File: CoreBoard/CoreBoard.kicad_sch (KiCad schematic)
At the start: 75 parts, among them J1 RJ45_LED_Shielded, SW1 SW_Push, SW10 SW_Push, SW12 SW_DIP_x07, SW2 SW_Push, SW3 SW_Push, SW4 SW_Push, SW5 SW_Push, SW6 SW_Push, SW7 SW_Push, SW8 SW_Push, SW9 SW_Push, U1 OKI, U2 Teensy4.1_DEV-16771, U3 SHHD003A0A, U4 GY-521, U5 ATA6561, U6 74HC148, U7 74HC148, U8 74HC00

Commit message: Fixed many things from schematic review, VCC power flags, no connects, added a 4th NAND gate, changed labels to text, changed DS8 tag to DS_EN, and removed the standby tag from the CAN transceiver to connect it to ground
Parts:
- added unit 4 of U8
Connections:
- net STBY is gone; now on net GND: U5.8 (STBY)
- net 5V: now also Conn2.1, U3.6 (Vout+)
- net DS8 renamed DS_EN
- net DS_EN: now also U6.12 (I2); no longer U2.10 (CS1)
- net DS9: no longer names the net of U2.36 (CS2)
- net DS9: no longer U6.12 (I2)
- net PV renamed VCC
- no-connect marks 18 -> 31
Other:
- note added: "Accelerometer"
- note added: "Encoders"
- note added: "Gimbal Buttons"
- note added: "NeoPixels"
- note added: "Power"
- note added: "Power LED"
- note added: "Servo Communication"
- note added: "Teensy"
- note added: "VESC Serial"
- moved on the sheet: U8E

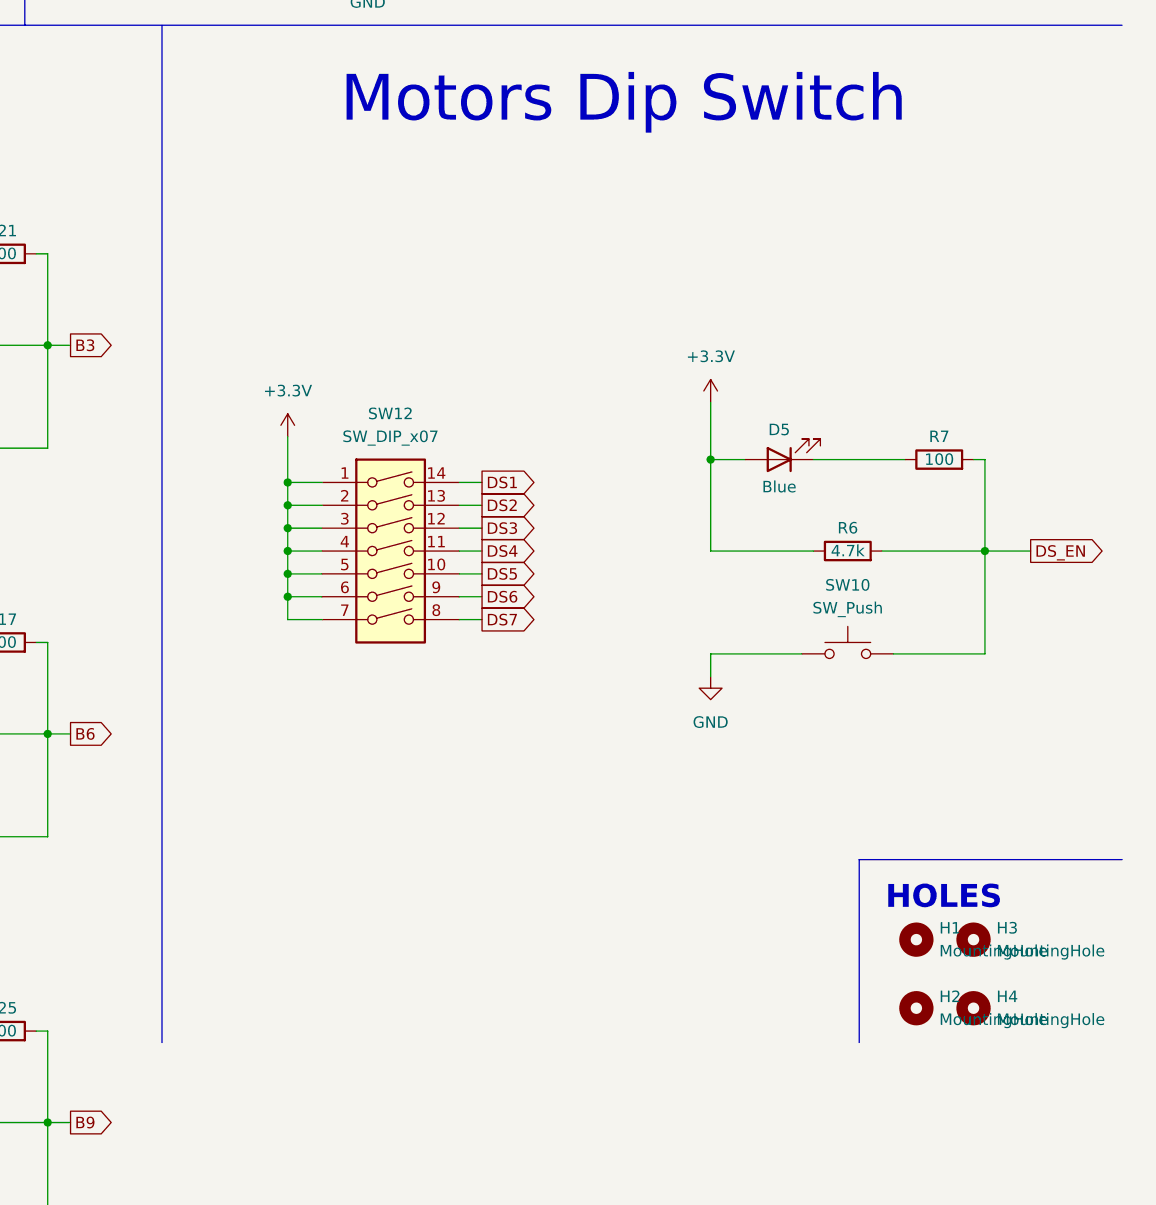
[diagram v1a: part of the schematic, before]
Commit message: Added CAN Connectors
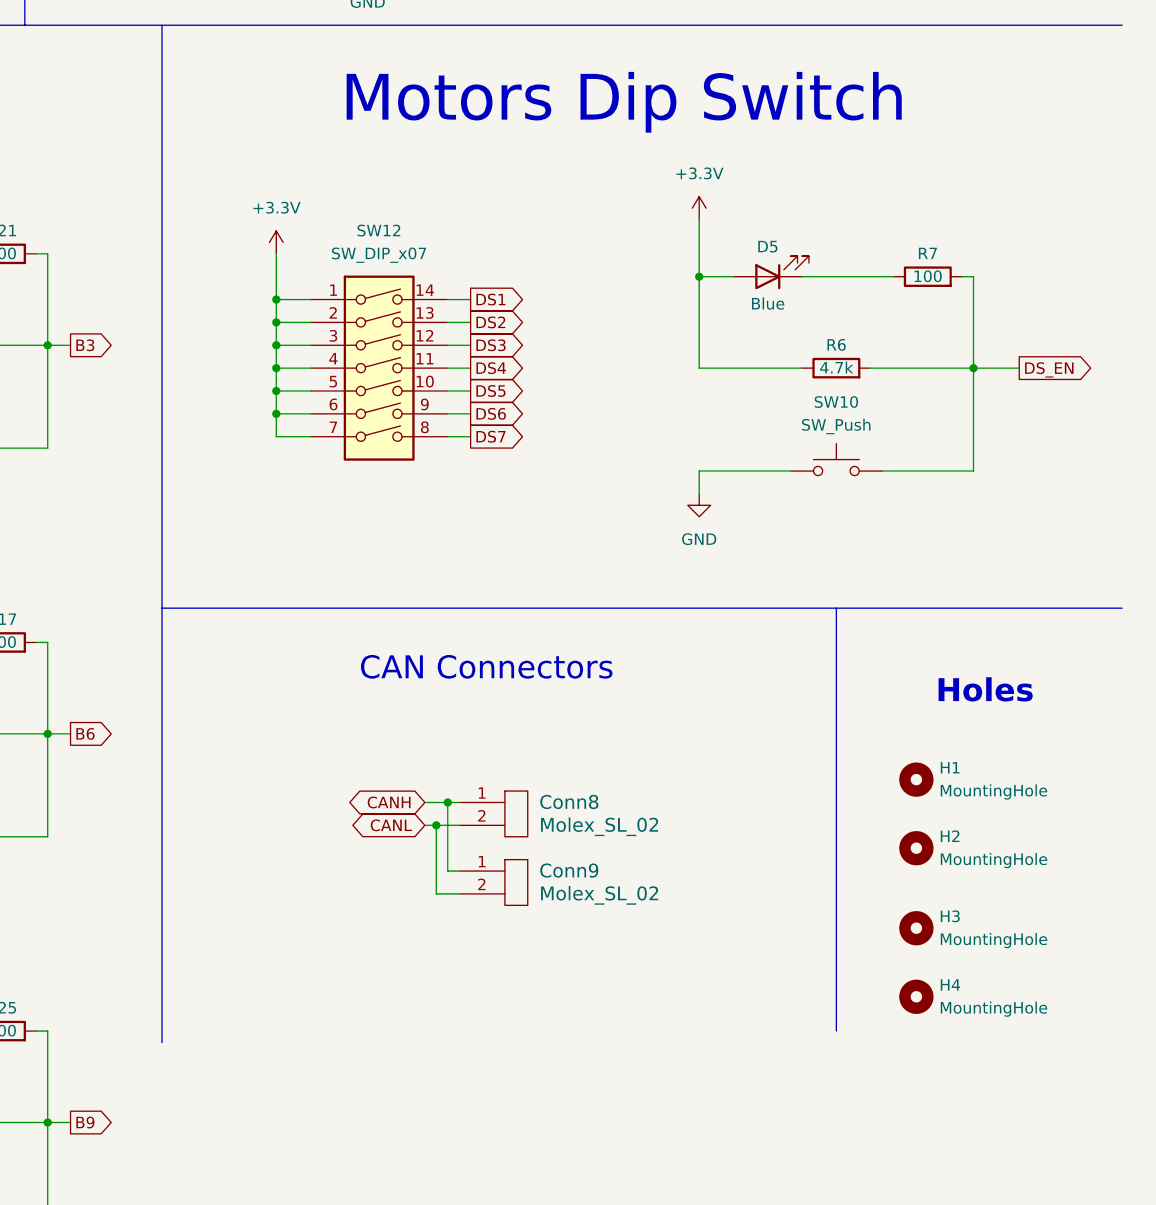
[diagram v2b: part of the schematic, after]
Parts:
- added Conn8, Conn9: Molex_SL_02, MRDT_Connectors:MOLEX_SL_02_Vertical, symbol MRDT_Connectors:Molex_SL_02
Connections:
- net CANH: now also Conn8.1, Conn9.1
- net CANL: now also Conn8.2, Conn9.2
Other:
- note added: "CAN Connectors"
- note added: "Holes"
- note removed: "HOLES"
- moved on the sheet: D5, H1, H2, H3, H4, R6, R7, SW10, SW12

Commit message: Added footprints to the majority of components on the schematic
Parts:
- C1: footprint (none) -> Capacitor_SMD:C_1206_3216Metric_Pad1.33x1.80mm_HandSolder
- C2, C3, C4, C5, C6: footprint (none) -> Capacitor_SMD:C_0603_1608Metric_Pad1.08x0.95mm_HandSolder
- Conn1: footprint (none) -> MRDT_Connectors:Square_Anderson_2_H_Side_By_Side_PV
- Conn2: footprint (none) -> MRDT_Connectors:MOLEX_SL_03_Vertical
- Conn3, Conn4, Conn5, Conn6, Conn7: footprint (none) -> MRDT_Connectors:MOLEX_SL_09_Horizontal
- D1, D10, D11, D12, D13, D2, D3, D4, D5, D6, D7, D8, D9: footprint (none) -> LED_SMD:LED_0603_1608Metric_Pad1.05x0.95mm_HandSolder
- J1: footprint (none) -> MRDT_Connectors:RJ45_Teensy
- R1, R10, R11, R12, R13, R14, R15, R16, R17, R18, R19, R2, R20, R21, R22, R23, R24, R25, R3, R4, R5, R6, R7, R8, R9: footprint (none) -> Resistor_SMD:R_0603_1608Metric_Pad0.98x0.95mm_HandSolder
- SW1, SW10, SW2, SW3, SW4, SW5, SW6, SW7, SW8, SW9: footprint (none) -> Button_Switch_SMD:SW_SPST_TL3305A
- U1: footprint (none) -> MRDT_Devices:OKI_Horizontal
- U2: footprint MODULE_DEV-16771 -> MRDT_Shields:Teensy_4_1_Ethernet
- U8: footprint (none) -> Package_SO:SO-14_5.3x10.2mm_P1.27mm

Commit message: Layout has been changed to group components together similar to the style of the schematic for better connections, and the footprint for the OKI for the NeoPixels has been changed
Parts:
- U3: footprint MRDT_Devices:SHHD003A0A-SRZ -> MRDT_Devices:SHHD003A0A-SRZ_Surface_Mount
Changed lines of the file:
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@@
 			)
 		)
-		(property "Footprint" "MRDT_Devices:SHHD003A0A-SRZ"
+		(property "Footprint" "MRDT_Devices:SHHD003A0A-SRZ_Surface_Mount"
 			(at 133.35 46.99 0)
 			(effects

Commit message: Added footprints for mounting holes
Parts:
- H1, H2, H3, H4: footprint (none) -> MRDT_Drill_Holes:4_40_Hole
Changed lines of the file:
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@@
 			)
 		)
-		(property "Footprint" ""
+		(property "Footprint" "MRDT_Drill_Holes:4_40_Hole"
 			(at 384.81 223.52 0)
 			(effects
@@
 			)
 		)
-		(property "Footprint" ""
+		(property "Footprint" "MRDT_Drill_Holes:4_40_Hole"
 			(at 384.81 240.03 0)
 			(effects
@@
 			)
 		)
-		(property "Footprint" ""
+		(property "Footprint" "MRDT_Drill_Holes:4_40_Hole"
 			(at 384.81 247.65 0)
 			(effects
@@
 			)
 		)
-		(property "Footprint" ""
+		(property "Footprint" "MRDT_Drill_Holes:4_40_Hole"
 			(at 384.81 231.14 0)
 			(effects

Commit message: Changed footprint of NeoPixels to a though hole, and added some wires
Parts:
- U3: footprint MRDT_Devices:SHHD003A0A-SRZ_Surface_Mount -> MRDT_Devices:SHHD003A0A41Z_Through_Hole
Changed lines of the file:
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@@
 			)
 		)
-		(property "Footprint" "MRDT_Devices:SHHD003A0A-SRZ_Surface_Mount"
+		(property "Footprint" "MRDT_Devices:SHHD003A0A41Z_Through_Hole"
 			(at 133.35 46.99 0)
 			(effects

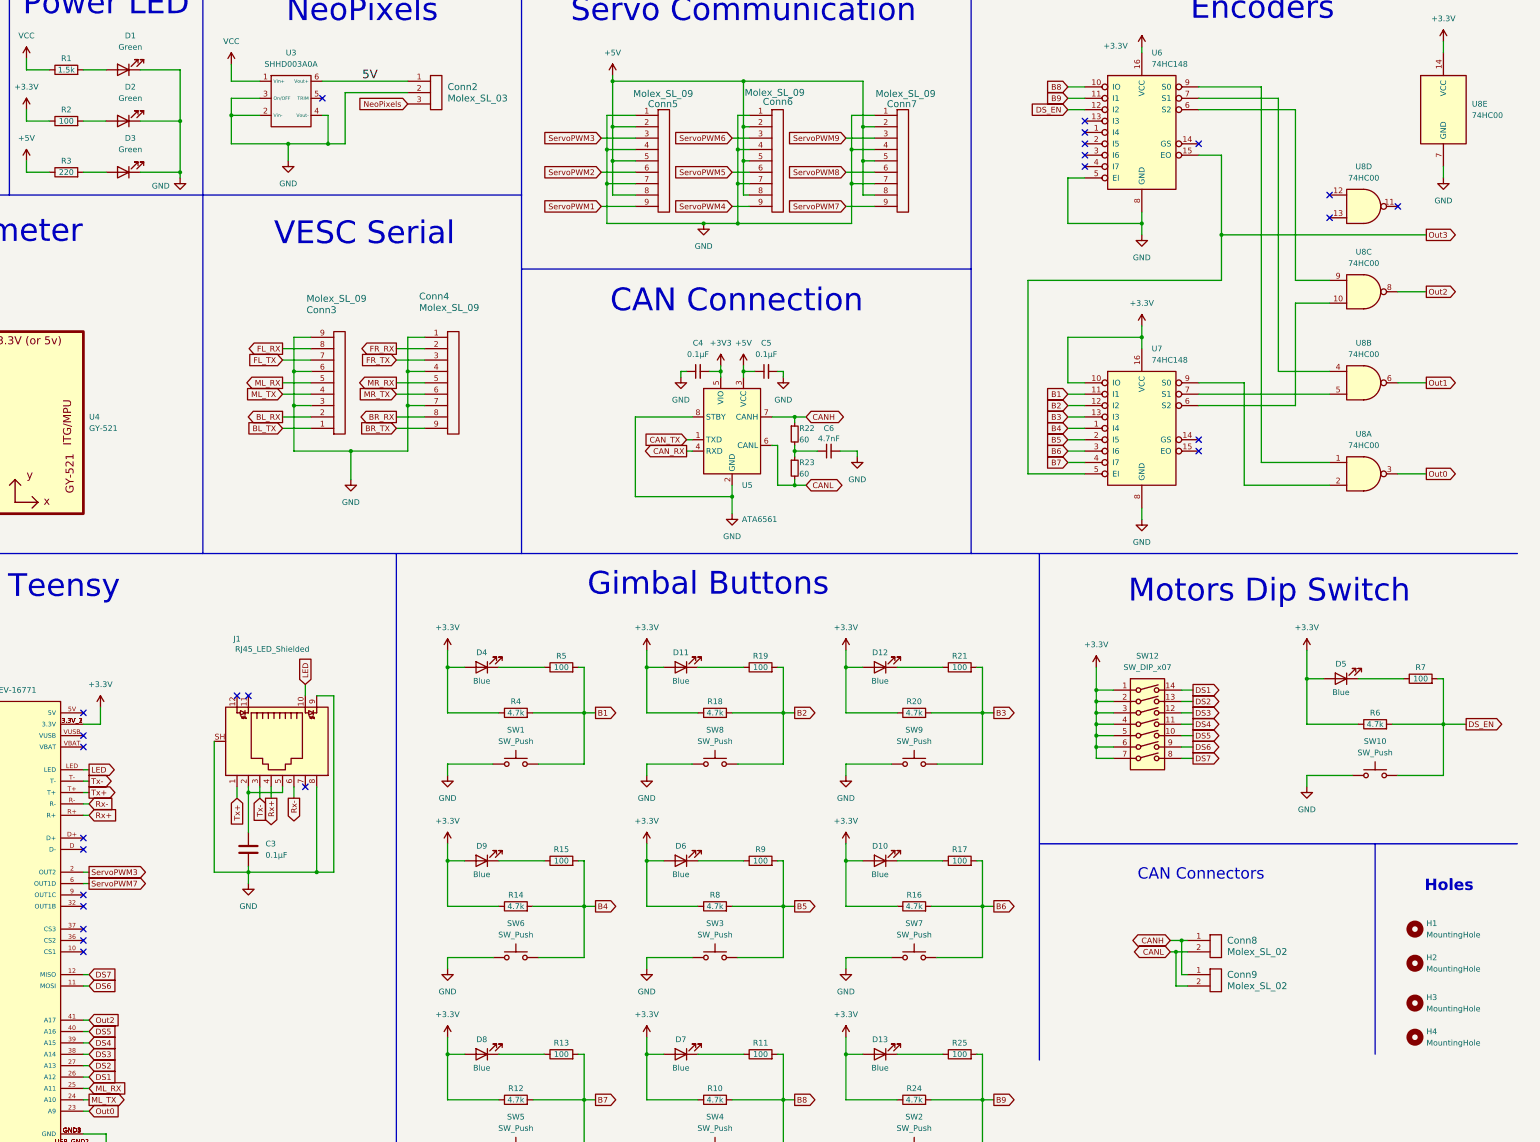
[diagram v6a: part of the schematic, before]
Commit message: Nearly completed first draft of the layout, and adjusted the schematic for easier routing
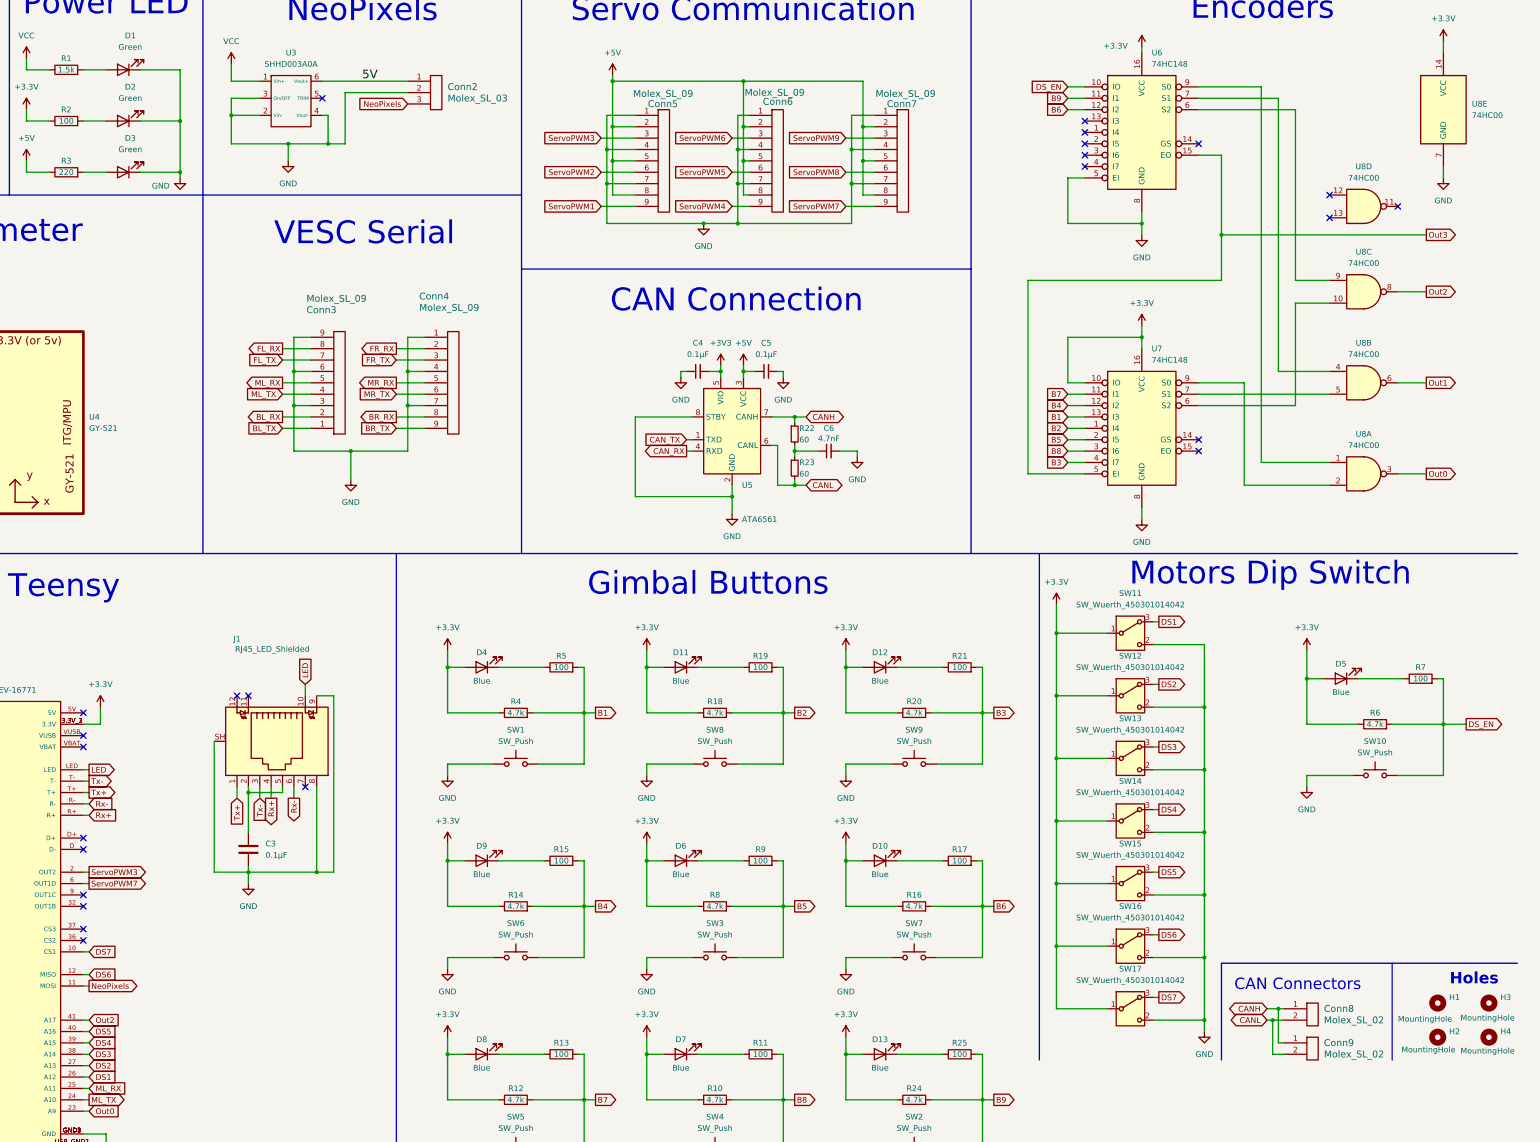
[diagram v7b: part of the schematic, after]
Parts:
- removed SW12: SW_DIP_x07, symbol Switch:SW_DIP_x07
- added SW11, SW12, SW13, SW14, SW15, SW16, SW17: SW_Wuerth_450301014042, MRDT_Switches:SW_Switch_03_STSSS9121_Through_Hole, symbol Switch:SW_Wuerth_450301014042
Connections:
- net +3.3V: now also SW11.1 (B), SW12.1 (B), SW13.1 (B), SW14.1 (B), SW15.1 (B), SW16.1 (B), SW17.1 (B)
- net B1: now also U7.13 (I3); no longer U7.11 (I1)
- net B2: now also U7.1 (I4); no longer U7.12 (I2)
- net B3: now also U7.4 (I7); no longer U7.13 (I3)
- net B4: now also U7.12 (I2); no longer U7.1 (I4)
- net B6: now also U6.12 (I2); no longer U7.3 (I6)
- net B7: now also U7.11 (I1); no longer U7.4 (I7)
- net B8: now also U7.3 (I6); no longer U6.10 (IO)
- net DS1: now also SW11.3 (A)
- net DS2: now also SW12.3 (A)
- net DS3: now also SW13.3 (A)
- net DS4: now also SW14.3 (A)
- net DS5: now also SW15.3 (A)
- net DS6: now also U2.12 (MISO), SW16.3 (A); no longer U2.11 (MOSI)
- net DS7: now also U2.10 (CS1), SW17.3 (A); no longer U2.12 (MISO)
- net DS_EN: now also U6.10 (IO); no longer U6.12 (I2)
- net GND: now also SW11.2 (C), SW12.2 (C), SW13.2 (C), SW14.2 (C), SW15.2 (C), SW16.2 (C), SW17.2 (C)
- net NeoPixels: now also U2.11 (MOSI)
- no-connect marks 31 -> 30
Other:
- moved on the sheet: Conn8, Conn9, H1, H2, H3, H4

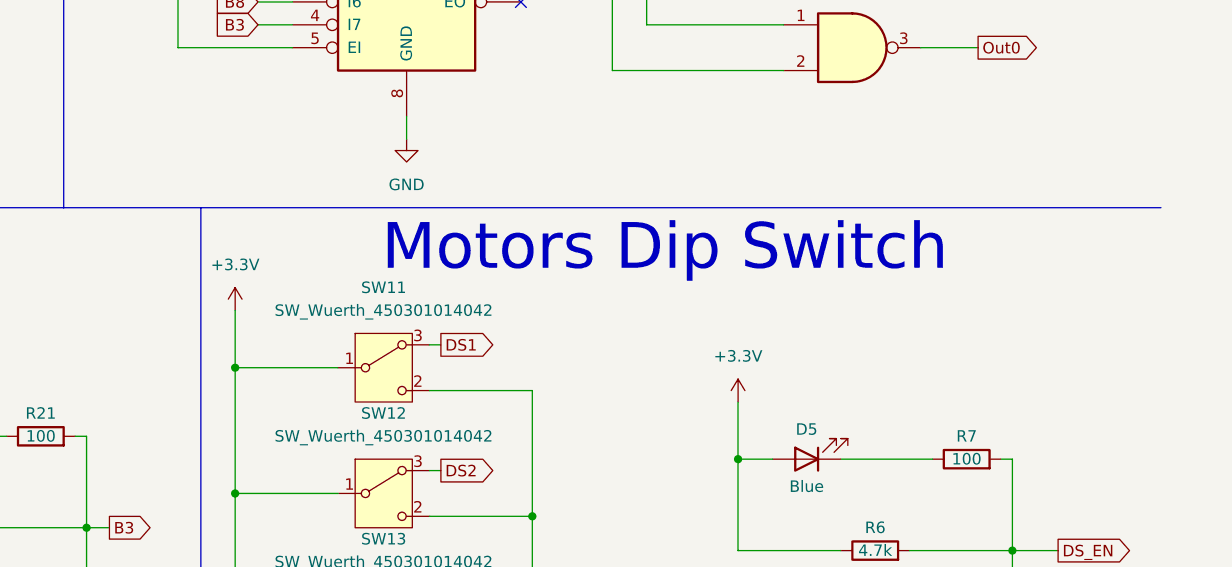
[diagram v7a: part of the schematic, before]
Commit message: Changed Schematic Heading for Switches
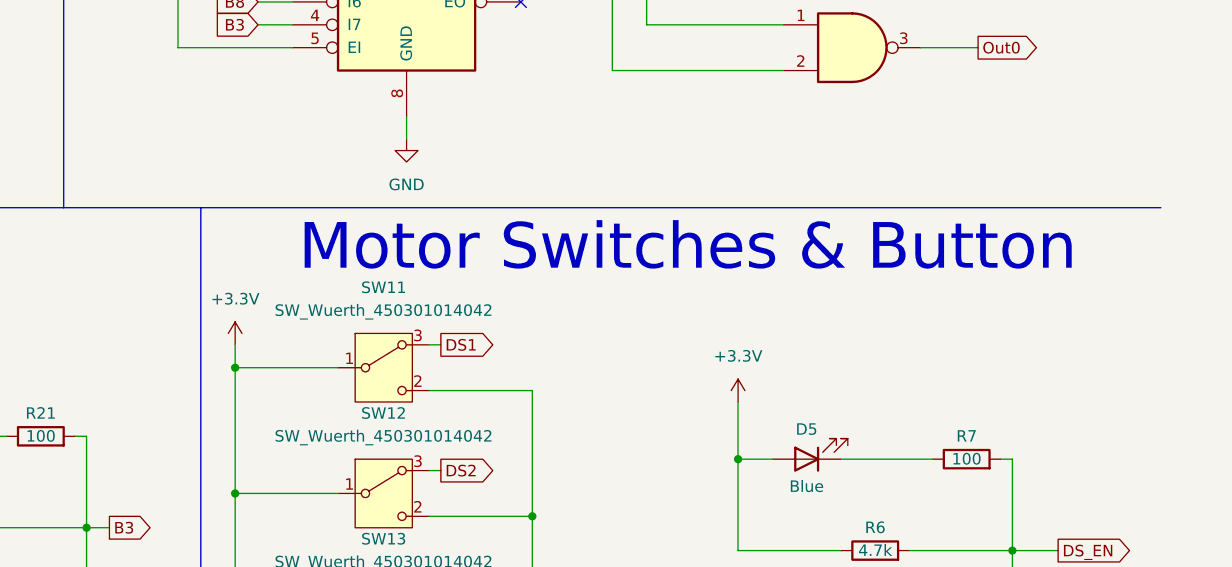
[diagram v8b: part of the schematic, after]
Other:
- note added: "Motor Switches & Button"
- note removed: "Motors Dip Switch"
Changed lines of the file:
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@@
 	(wire
 		(pts
-			(xy 304.8 151.13) (xy 304.8 157.48)
+			(xy 304.8 154.94) (xy 304.8 157.48)
 		)
 		(stroke
@@
 		)
 	)
-	(text "Motors Dip Switch"
+	(text "Motor Switches & Button"
 		(exclude_from_sim no)
-		(at 352.552 144.272 0)
+		(at 355.092 144.272 0)
 		(effects
 			(font
@@
 	(symbol
 		(lib_id "power:+3.3V")
-		(at 304.8 151.13 0)
+		(at 304.8 154.94 0)
 		(unit 1)
 		(exclude_from_sim no)
@@
 		(fields_autoplaced yes)
 		(property "Reference" "#PWR012"
-			(at 304.8 154.94 0)
+			(at 304.8 158.75 0)
 			(effects
 				(font
@@
 		)
 		(property "Value" "+3.3V"
-			(at 304.8 146.05 0)
+			(at 304.8 149.86 0)
 			(effects
 				(font
@@
 		)
 		(property "Footprint" ""
-			(at 304.8 151.13 0)
+			(at 304.8 154.94 0)
 			(effects
 				(font
@@
 		)
 		(property "Datasheet" ""
-			(at 304.8 151.13 0)
+			(at 304.8 154.94 0)
 			(effects
 				(font
@@
 		)
 		(property "Description" "Power symbol creates a global label with name \"+3.3V\""
-			(at 304.8 151.13 0)
+			(at 304.8 154.94 0)
 			(effects
 				(font
